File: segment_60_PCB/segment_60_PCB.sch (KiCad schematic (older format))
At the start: 131 parts, among them J1 BREAKOUT, SW1 SW_Push_45deg, SW10 SW_Push_45deg, SW11 SW_Push_45deg, SW12 SW_Push_45deg, SW13 SW_Push_45deg, SW14 SW_Push_45deg, SW15 SW_Push_45deg, SW16 SW_Push_45deg, SW17 SW_Push_45deg, SW18 SW_Push_45deg, SW19 SW_Push_45deg, SW2 SW_Push_45deg, SW20 SW_Push_45deg, SW21 SW_Push_45deg, SW22 SW_Push_45deg, SW23 SW_Push_45deg, SW24 SW_Push_45deg, SW25 SW_Push_45deg, SW26 SW_Push_45deg, SW27 SW_Push_45deg, SW28 SW_Push_45deg, SW29 SW_Push_45deg, SW3 SW_Push_45deg, SW30 SW_Push_45deg, SW31 SW_Push_45deg, SW32 SW_Push_45deg, SW33 SW_Push_45deg, SW34 SW_Push_45deg, SW35 SW_Push_45deg, SW36 SW_Push_45deg, SW37 SW_Push_45deg, SW38 SW_Push_45deg, SW39 SW_Push_45deg, SW4 SW_Push_45deg, SW40 SW_Push_45deg, SW41 SW_Push_45deg, SW42 SW_Push_45deg, SW43 SW_Push_45deg, SW44 SW_Push_45deg, SW45 SW_Push_45deg, SW46 SW_Push_45deg, SW47 SW_Push_45deg, SW48 SW_Push_45deg, SW49 SW_Push_45deg, SW5 SW_Push_45deg, SW50 SW_Push_45deg, SW51 SW_Push_45deg, SW52 SW_Push_45deg, SW53 SW_Push_45deg, SW54 SW_Push_45deg, SW55 SW_Push_45deg, SW56 SW_Push_45deg, SW57 SW_Push_45deg, SW58 SW_Push_45deg, SW59 SW_Push_45deg, SW6 SW_Push_45deg, SW60 SW_Push_45deg, SW61 SW_Push_45deg, SW62 SW_Push_45deg, SW63 SW_Push_45deg, SW64 SW_Push_45deg, SW65 SW_Push_45deg, SW66 SW_Push, SW67 SW_Push, SW7 SW_Push_45deg, SW8 SW_Push_45deg, SW9 SW_Push_45deg, U1 ATmega328P-PU, U10 74HC365, U11 74HC365, U12 74HC365, U13 74HC365, U14 74HC365, U15 74HC365, U16 74HC365, U17 74HC365, U2 74HC138, U3 74HC138, U4 74HC365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

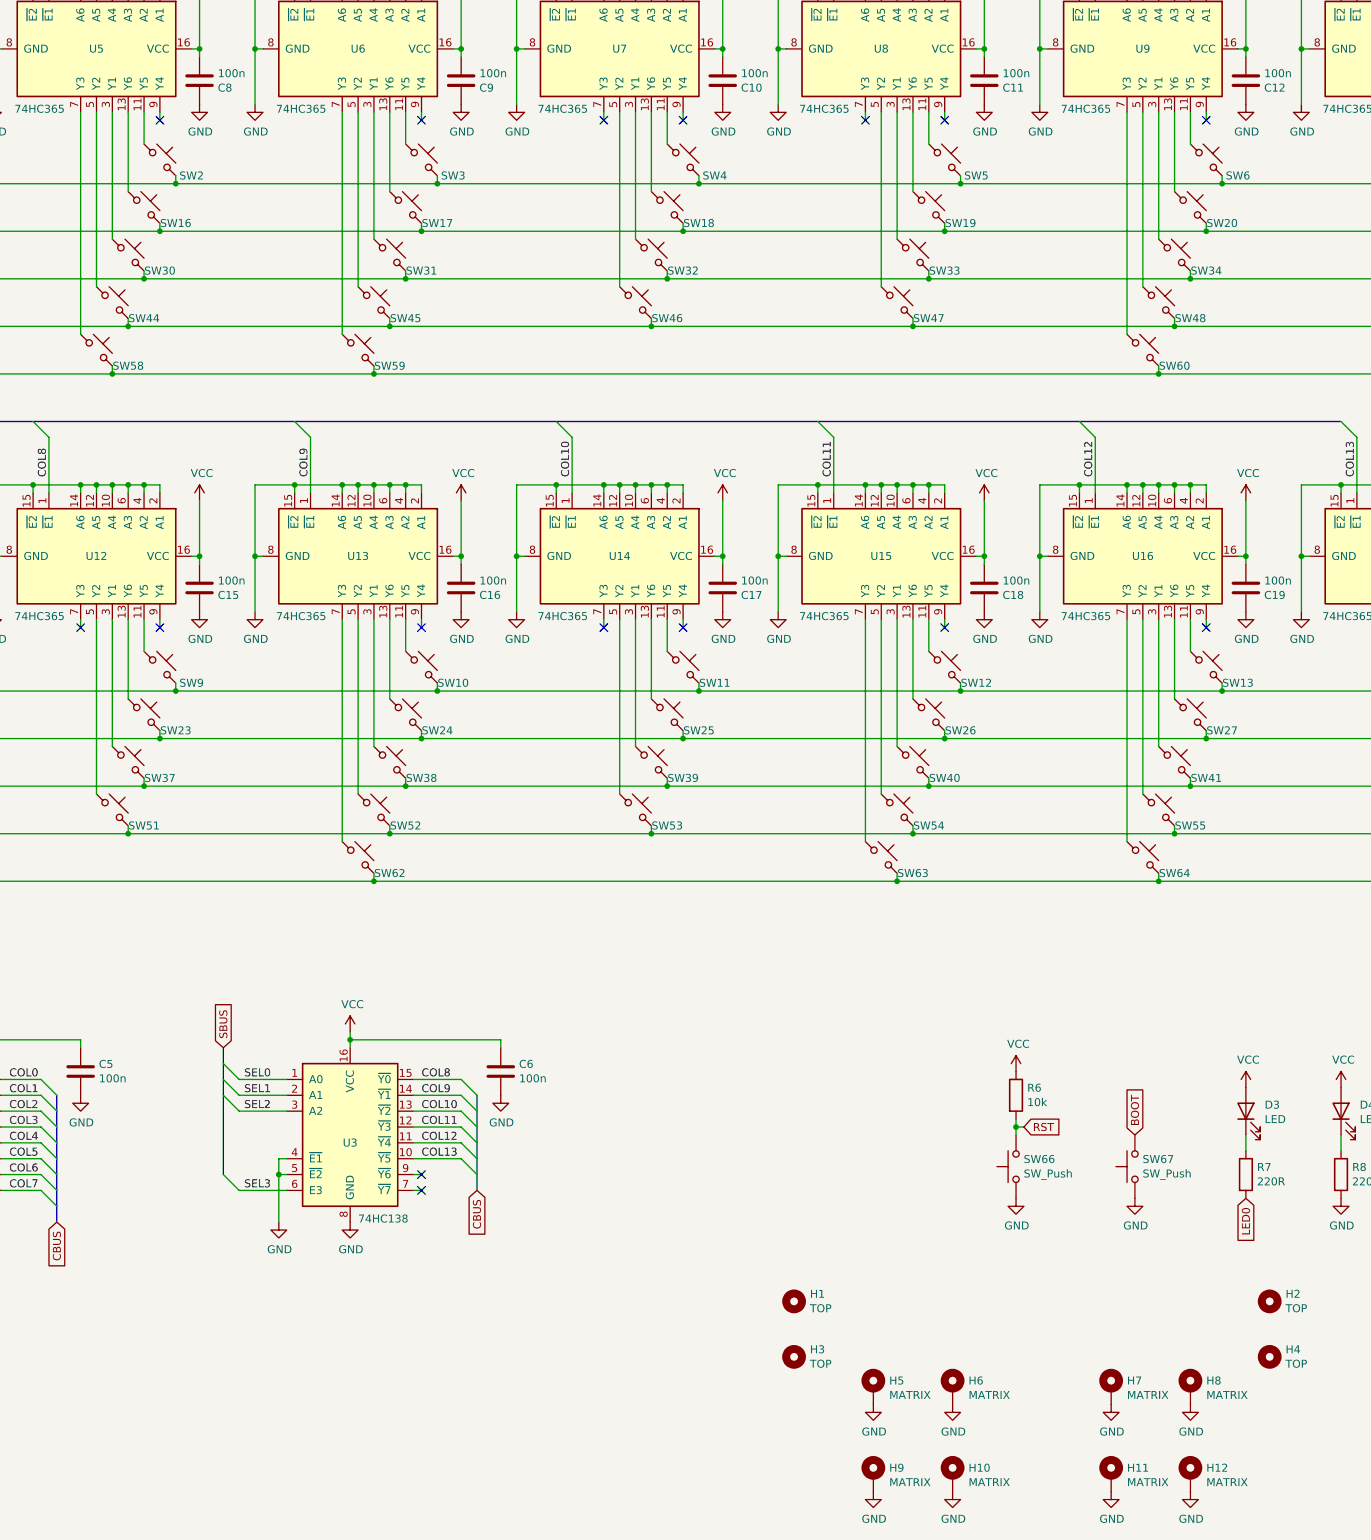
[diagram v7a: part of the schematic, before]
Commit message: Routed first 8 columns of switches
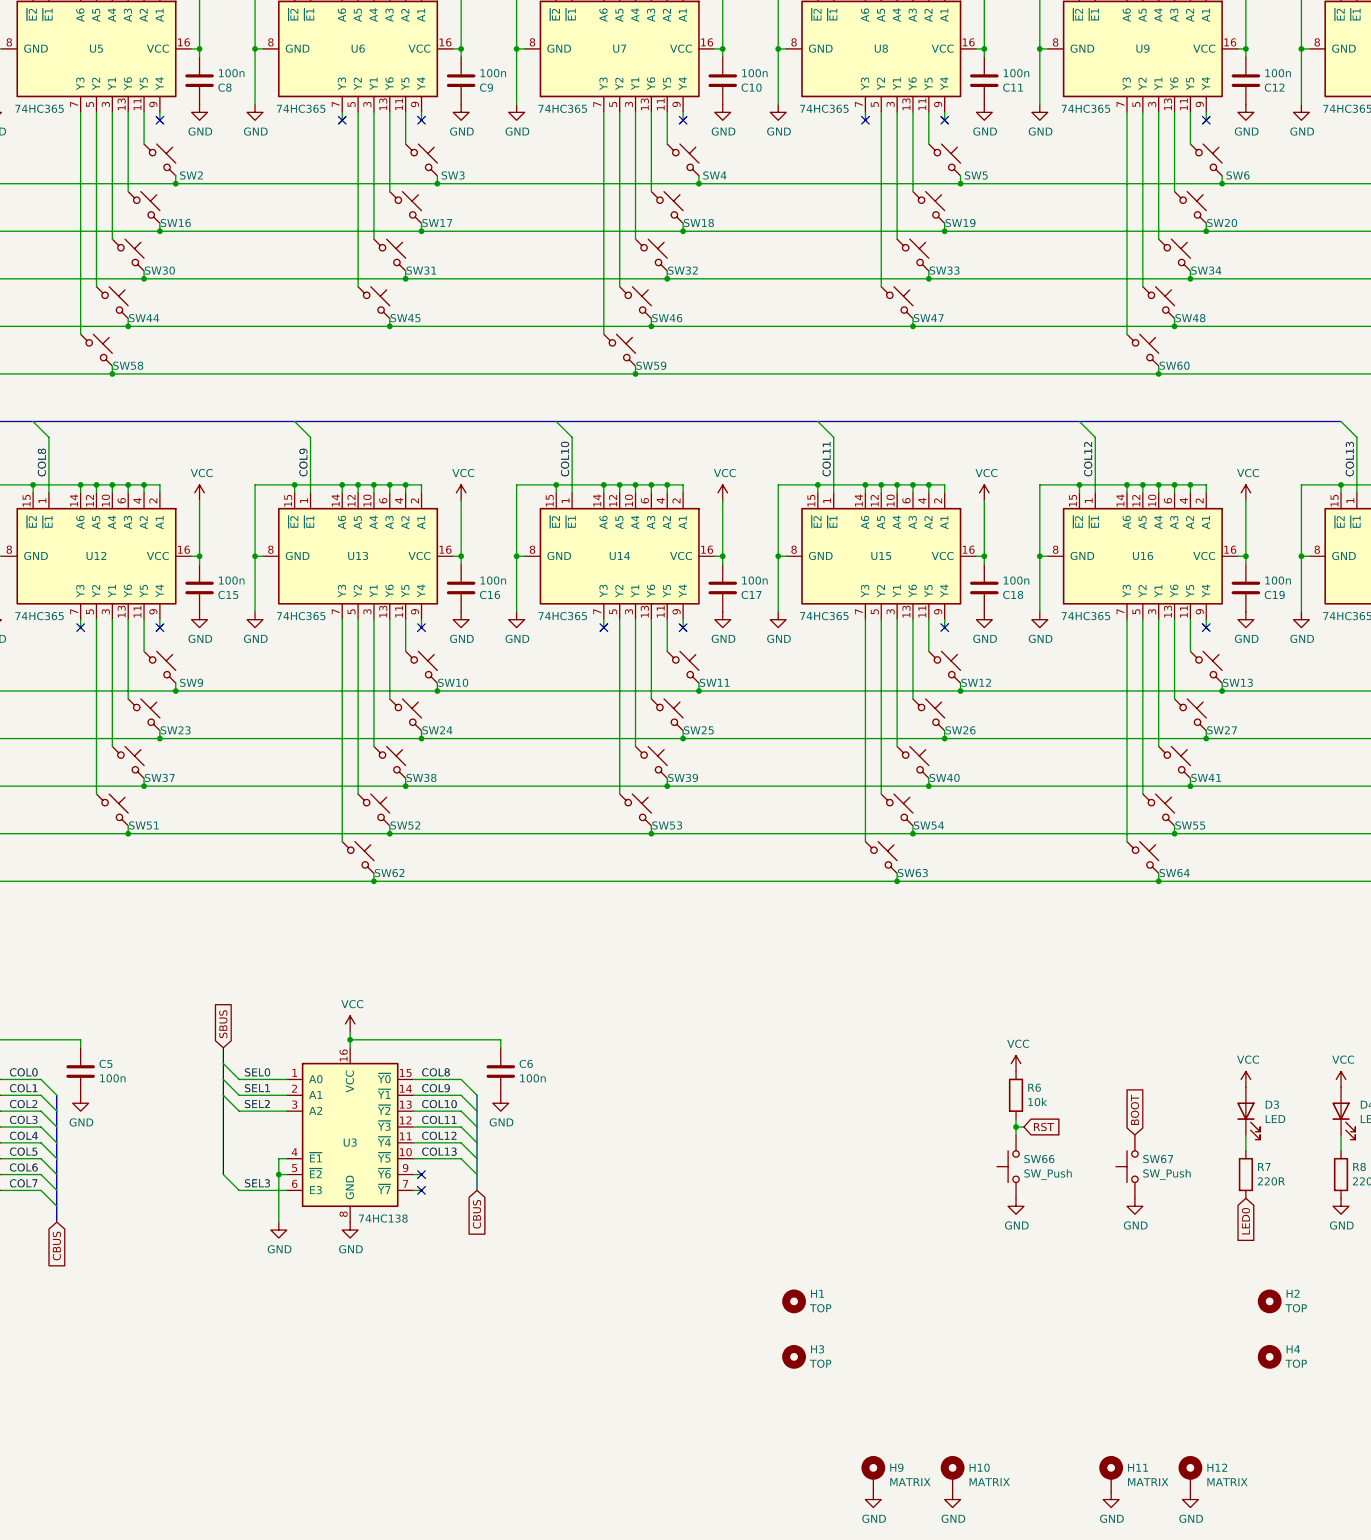
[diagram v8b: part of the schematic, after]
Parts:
- removed H5, H6, H7, H8: MATRIX, MountingHole:MountingHole_3.2mm_M3_Pad, symbol Mechanical:MountingHole_Pad
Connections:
- net at U6.7 (Y3): no longer SW59.1
- net at U7.7 (Y3): now also SW59.1
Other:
- moved on the sheet: SW59
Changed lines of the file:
@@
 	4750 2000 4750 3100
 Wire Wire Line
-	4650 2000 4650 3400
-Wire Wire Line
 	5050 3000 5050 3050
 Wire Wire Line
 	4950 3300 4950 3350
 Wire Wire Line
-	4850 3600 4850 3650
-Wire Wire Line
 	6700 2200 6700 2000
 Wire Wire Line
@@
 	3300 3350 4950 3350
 Wire Wire Line
-	3200 3650 4850 3650
-Wire Wire Line
 	6900 2450 8550 2450
 Wire Wire Line
@@
 Connection ~ 3500 2750
 Connection ~ 3600 2450
-Connection ~ 4850 3650
 Connection ~ 4950 3350
 Connection ~ 5050 3050
@@
 L Switch:SW_Push_45deg SW59
 U 1 1 66417B31
-P 4750 3500
+P 6400 3500
 AR Path="/66417B31" Ref="SW59"  Part="1"
 AR Path="/61CA4571/66417B31" Ref="SW?"  Part="1"
-F 0 "SW59" H 4950 3400 50  0000 C CNN
-F 1 "SW_Push_45deg" H 4750 3690 50  0001 C CNN
-F 2 "Segment_Footprints:Segment_MX_1.50u_PCB" H 4750 3500 50  0001 C CNN
-F 3 "~" H 4750 3500 50  0001 C CNN
-	1    4750 3500
+F 0 "SW59" H 6600 3400 50  0000 C CNN
+F 1 "SW_Push_45deg" H 6400 3690 50  0001 C CNN
+F 2 "Segment_Footprints:Segment_MX_1.50u_PCB" H 6400 3500 50  0001 C CNN
+F 3 "~" H 6400 3500 50  0001 C CNN
+	1    6400 3500
 	1    0    0    -1
 $EndComp
@@
 	4850 6850 8150 6850
 Wire Wire Line
-	4850 3650 9800 3650
-Wire Wire Line
 	3000 5200 3000 5250
 NoConn ~ 3000 5250
@@
 NoConn ~ 6300 5250
 Wire Wire Line
-	6300 2000 6300 2050
-NoConn ~ 6300 2050
-Wire Wire Line
 	7950 2000 7950 2050
 NoConn ~ 7950 2050
@@
 $EndComp
 $Comp
-L Mechanical:MountingHole_Pad H5
-U 1 1 61F83D8C
-P 8000 10050
-F 0 "H5" H 8100 10099 50  0000 L CNN
-F 1 "MATRIX" H 8100 10008 50  0000 L CNN
-F 2 "MountingHole:MountingHole_3.2mm_M3_Pad" H 8000 10050 50  0001 C CNN
-F 3 "~" H 8000 10050 50  0001 C CNN
-	1    8000 10050
-	1    0    0    -1
-$EndComp
-$Comp
 L Mechanical:MountingHole_Pad H9
 U 1 1 6203E4F6
@@
 $EndComp
 $Comp
-L power:GND #PWR09
-U 1 1 6203E7B5
-P 8000 10150
-F 0 "#PWR09" H 8000 9900 50  0001 C CNN
-F 1 "GND" H 8005 9977 50  0000 C CNN
-F 2 "" H 8000 10150 50  0001 C CNN
-F 3 "" H 8000 10150 50  0001 C CNN
-	1    8000 10150
-	1    0    0    -1
-$EndComp
-$Comp
 L power:GND #PWR013
 U 1 1 6203EB44
@@
 $EndComp
 $Comp
-L Mechanical:MountingHole_Pad H6
-U 1 1 620989E5
-P 8500 10050
-F 0 "H6" H 8600 10099 50  0000 L CNN
-F 1 "MATRIX" H 8600 10008 50  0000 L CNN
-F 2 "MountingHole:MountingHole_3.2mm_M3_Pad" H 8500 10050 50  0001 C CNN
-F 3 "~" H 8500 10050 50  0001 C CNN
-	1    8500 10050
-	1    0    0    -1
-$EndComp
-$Comp
 L Mechanical:MountingHole_Pad H10
 U 1 1 620989EB
@@
 $EndComp
 $Comp
-L power:GND #PWR010
-U 1 1 620989F1
-P 8500 10150
-F 0 "#PWR010" H 8500 9900 50  0001 C CNN
-F 1 "GND" H 8505 9977 50  0000 C CNN
-F 2 "" H 8500 10150 50  0001 C CNN
-F 3 "" H 8500 10150 50  0001 C CNN
-	1    8500 10150
-	1    0    0    -1
-$EndComp
-$Comp
 L power:GND #PWR069
 U 1 1 620989F7
@@
 $EndComp
 $Comp
-L Mechanical:MountingHole_Pad H7
-U 1 1 620F22C5
-P 9500 10050
-F 0 "H7" H 9600 10099 50  0000 L CNN
-F 1 "MATRIX" H 9600 10008 50  0000 L CNN
-F 2 "MountingHole:MountingHole_3.2mm_M3_Pad" H 9500 10050 50  0001 C CNN
-F 3 "~" H 9500 10050 50  0001 C CNN
-	1    9500 10050
-	1    0    0    -1
-$EndComp
-$Comp
 L Mechanical:MountingHole_Pad H11
 U 1 1 620F22CB
@@
 $EndComp
 $Comp
-L power:GND #PWR011
-U 1 1 620F22D1
-P 9500 10150
-F 0 "#PWR011" H 9500 9900 50  0001 C CNN
-F 1 "GND" H 9505 9977 50  0000 C CNN
-F 2 "" H 9500 10150 50  0001 C CNN
-F 3 "" H 9500 10150 50  0001 C CNN
-	1    9500 10150
-	1    0    0    -1
-$EndComp
-$Comp
 L power:GND #PWR071
 U 1 1 620F22D7
@@
 $EndComp
 $Comp
-L Mechanical:MountingHole_Pad H8
-U 1 1 620F22DD
-P 10000 10050
-F 0 "H8" H 10100 10099 50  0000 L CNN
-F 1 "MATRIX" H 10100 10008 50  0000 L CNN
-F 2 "MountingHole:MountingHole_3.2mm_M3_Pad" H 10000 10050 50  0001 C CNN
-F 3 "~" H 10000 10050 50  0001 C CNN
-	1    10000 10050
-	1    0    0    -1
-$EndComp
-$Comp
 L Mechanical:MountingHole_Pad H12
 U 1 1 620F22E3
@@
 $EndComp
 $Comp
-L power:GND #PWR012
-U 1 1 620F22E9
-P 10000 10150
-F 0 "#PWR012" H 10000 9900 50  0001 C CNN
-F 1 "GND" H 10005 9977 50  0000 C CNN
-F 2 "" H 10000 10150 50  0001 C CNN
-F 3 "" H 10000 10150 50  0001 C CNN
-	1    10000 10150
-	1    0    0    -1
-$EndComp
-$Comp
 L power:GND #PWR072
 U 1 1 620F22EF
@@
 	13500 8700 13500 8650
 Connection ~ 13500 8700
+Wire Wire Line
+	3200 3650 6500 3650
+Wire Wire Line
+	4650 2000 4650 2050
+NoConn ~ 4650 2050
+Wire Wire Line
+	6300 2000 6300 3400
+Wire Wire Line
+	6500 3600 6500 3650
 Wire Bus Line
 	15050 3550 15050 3950
@@
 Wire Bus Line
 	2850 8200 2850 9000
+Connection ~ 6500 3650
+Wire Wire Line
+	6500 3650 9800 3650
 $EndSCHEMATC
